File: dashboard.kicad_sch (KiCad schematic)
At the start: 8 parts, among them SW1 SW_Push, SW3 SW_Push, SW4 SW_Push

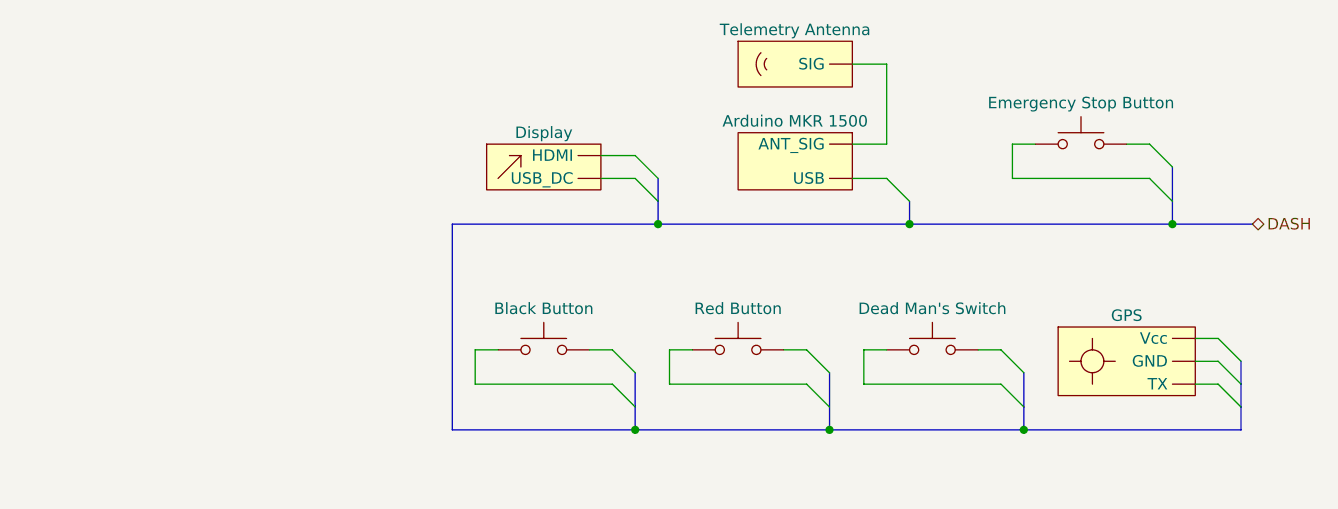
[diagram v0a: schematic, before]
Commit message: Add labels
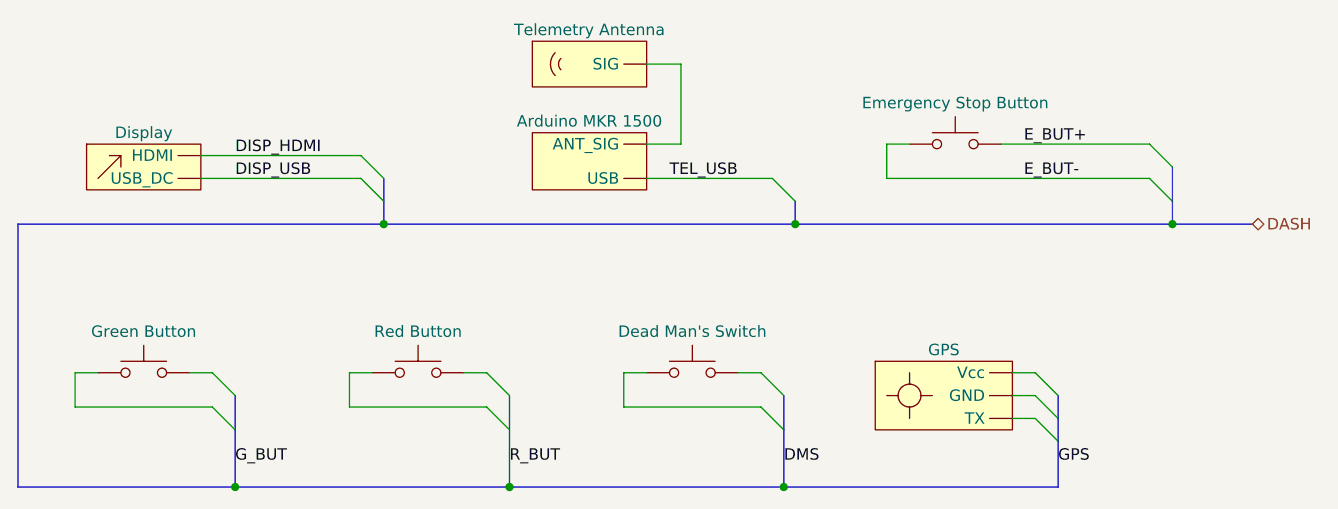
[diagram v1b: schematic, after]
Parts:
- SW3: Name Black Button -> Green Button
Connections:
- net DISP_USB: now reaches DSP1. (USB_DC)
- net E_BUT-: now reaches SW1.1
- net E_BUT+: now reaches SW1.2
- net TEL_USB: now reaches ARD1. (USB)
- new net DISP_HDMI: DSP1. (USB_DC)
